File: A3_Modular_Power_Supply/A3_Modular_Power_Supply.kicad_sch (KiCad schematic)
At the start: 73 parts, among them J1 JST-XH, J10 JST-XH, J11 JST-XH, J12 JST-XH, J13 JST-XH, J14 JST-XH, J15 JST-XH, J16 JST-XH, J17 FX30B-3P-7.62DSA, J18 FX30B-3S-7.62DSA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

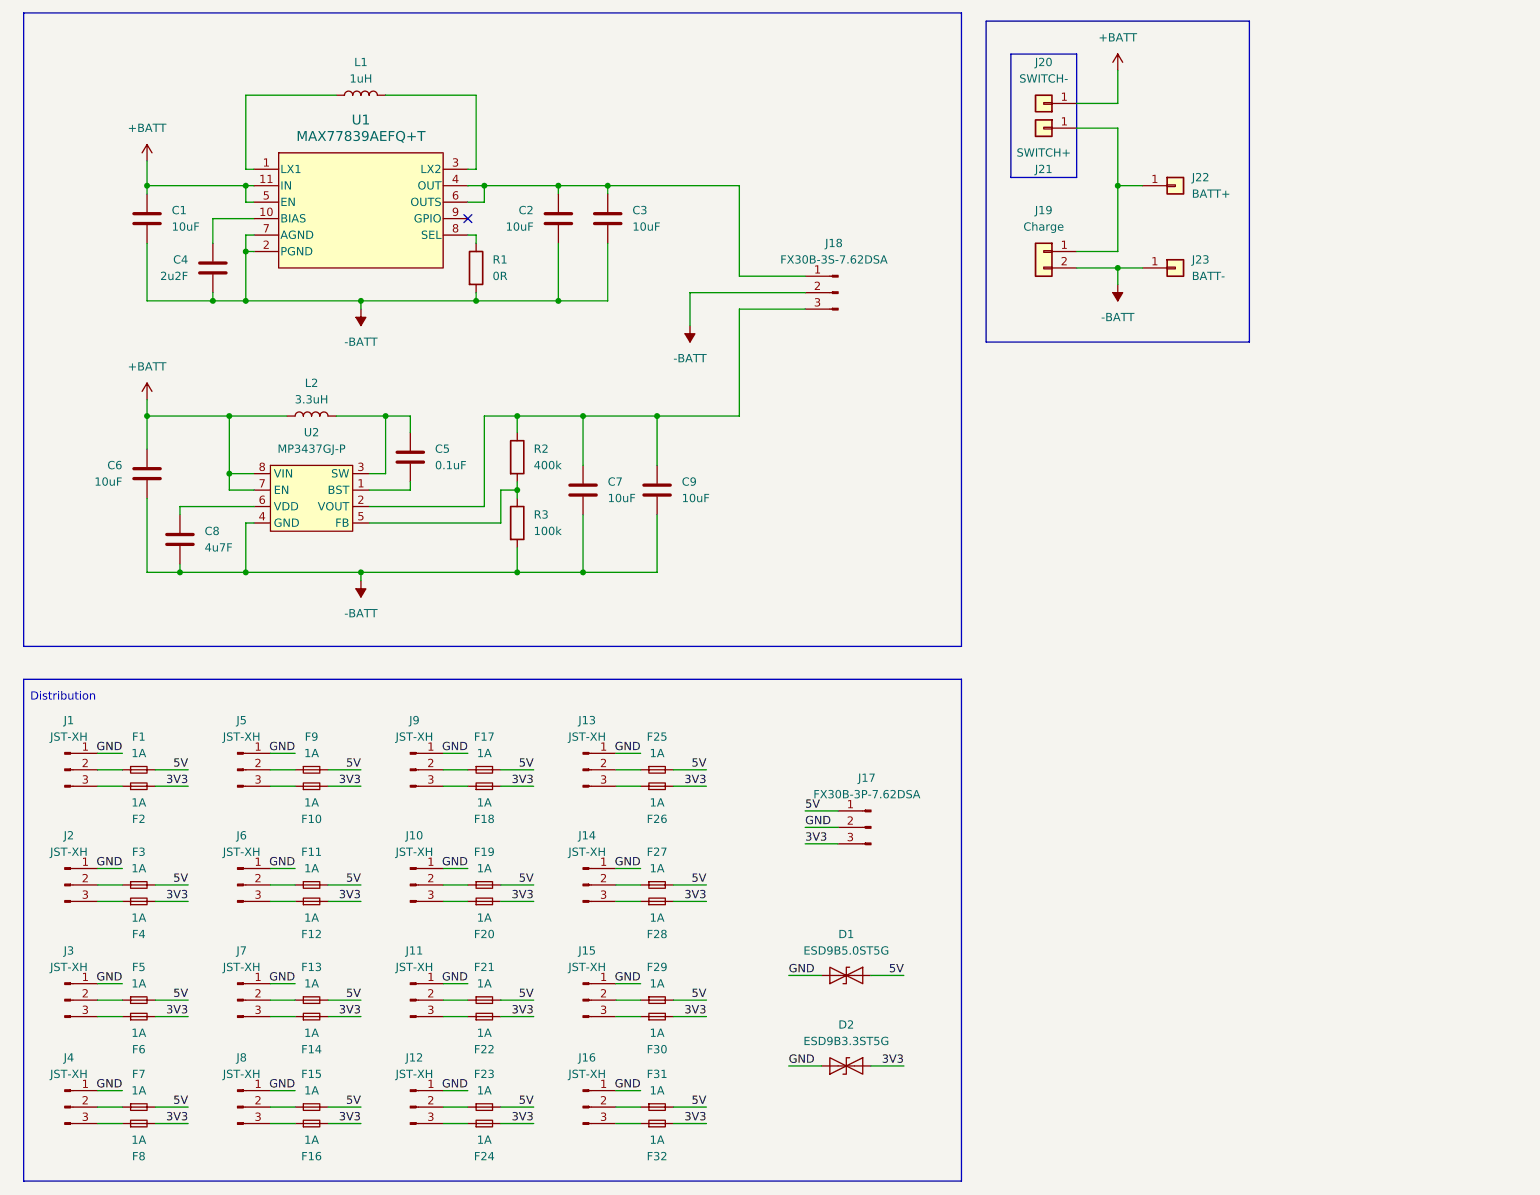
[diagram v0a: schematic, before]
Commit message: Resized board to match flight computer Switched to single PCB
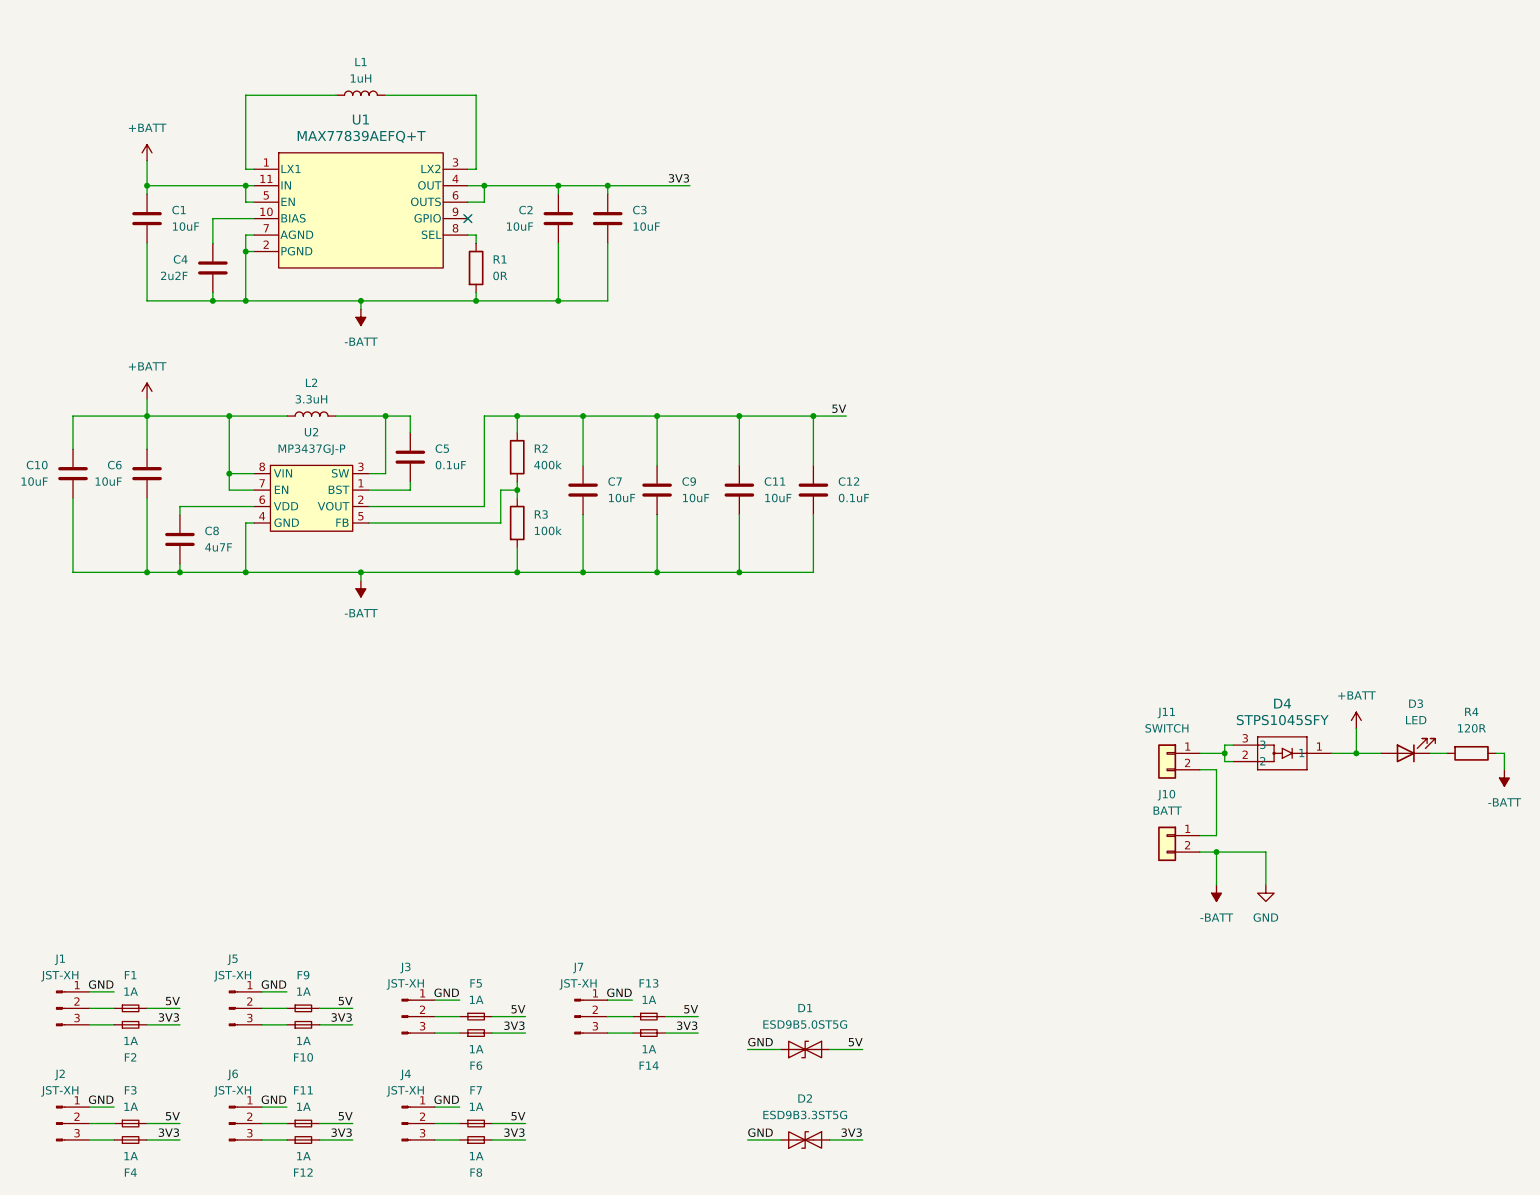
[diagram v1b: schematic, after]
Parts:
- removed F15, F16, F17, F18, F19, F20, F21, F22, F23, F24, F25, F26, F27, F28, F29, F30, F31, F32: 1A, Fuse:Fuse_0603_1608Metric, symbol Device:Fuse_Small
- removed J10, J11, J12, J13, J14, J15, J16, J8, J9: JST-XH, Connector_JST:JST_XH_B3B-XH-A_1x03_P2.50mm_Vertical, symbol Connector:Conn_01x03_Pin
- removed J17: FX30B-3P-7.62DSA, MPS_footprints:FX30B-3x-7.62, symbol Connector:Conn_01x03_Pin
- removed J18: FX30B-3S-7.62DSA, MPS_footprints:FX30B-3x-7.62, symbol Connector:Conn_01x03_Pin
- removed J20: SWITCH-, Connector_Wire:SolderWire-1.5sqmm_1x01_D1.7mm_OD3.9mm, symbol Connector_Generic:Conn_01x01
- removed J21: SWITCH+, Connector_Wire:SolderWire-1.5sqmm_1x01_D1.7mm_OD3.9mm, symbol Connector_Generic:Conn_01x01
- removed J22: BATT+, MPS_footprints:Nickle_Strip, symbol Connector_Generic:Conn_01x01
- removed J23: BATT-, MPS_footprints:Nickle_Strip, symbol Connector_Generic:Conn_01x01
- added C10, C11: 10uF, Capacitor_SMD:C_1206_3216Metric, symbol Device:C
- added C12: 0.1uF, Capacitor_SMD:C_0603_1608Metric, symbol Device:C
- added D3: LED, LED_SMD:LED_0603_1608Metric, symbol Device:LED
- added D4: STPS1045SFY, PSMCTO-277A_STM, symbol MPS_symbols:STPS1045SFY
- added J11: SWITCH, Connector_JST:JST_VH_B2PS-VH_1x02_P3.96mm_Horizontal, symbol Connector_Generic:Conn_01x02
- added R4: 120R, Resistor_SMD:R_0603_1608Metric, symbol Device:R
- J1, J2, J3, J4, J5, J6, J7: footprint Connector_JST:JST_XH_B3B-XH-A_1x03_P2.50mm_Vertical -> Connector_JST:JST_XH_S3B-XH-A_1x03_P2.50mm_Horizontal
- J10: renamed from J19; value Charge -> BATT
- L2: footprint Inductor_SMD:L_Bourns_SRP1245A -> MPS_footprints:L_Wurth_WE-XHMI-6060P
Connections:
- net GND is gone; now on net -BATT: D1.2 (A2), D2.1 (A1), J1.1 (Pin_1), J2.1 (Pin_1), J3.1 (Pin_1), J4.1 (Pin_1), J5.1 (Pin_1), J6.1 (Pin_1), J7.1 (Pin_1)
- net +BATT: now also C10.1, D3.2 (A), D4.1
- net -BATT: now also C10.2, C11.2, C12.2, R4.1
- net 3V3: now also C2.1, C3.1, U1.4 (OUT), U1.6 (OUTS)
- net 5V: now also C7.1, C9.1, R2.1, U2.2 (VOUT), C11.1, C12.1
- net at J10.1 (Pin_1): now also J11.2 (Pin_2)
- new net: D3.1 (K), R4.2
- new net: D4.2, D4.3, J11.1 (Pin_1)
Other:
- note removed: "Distribution"
- moved on the sheet: D1, D2, F1, F10, F11, F12, F13, F14, F2, F3, F4, F5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

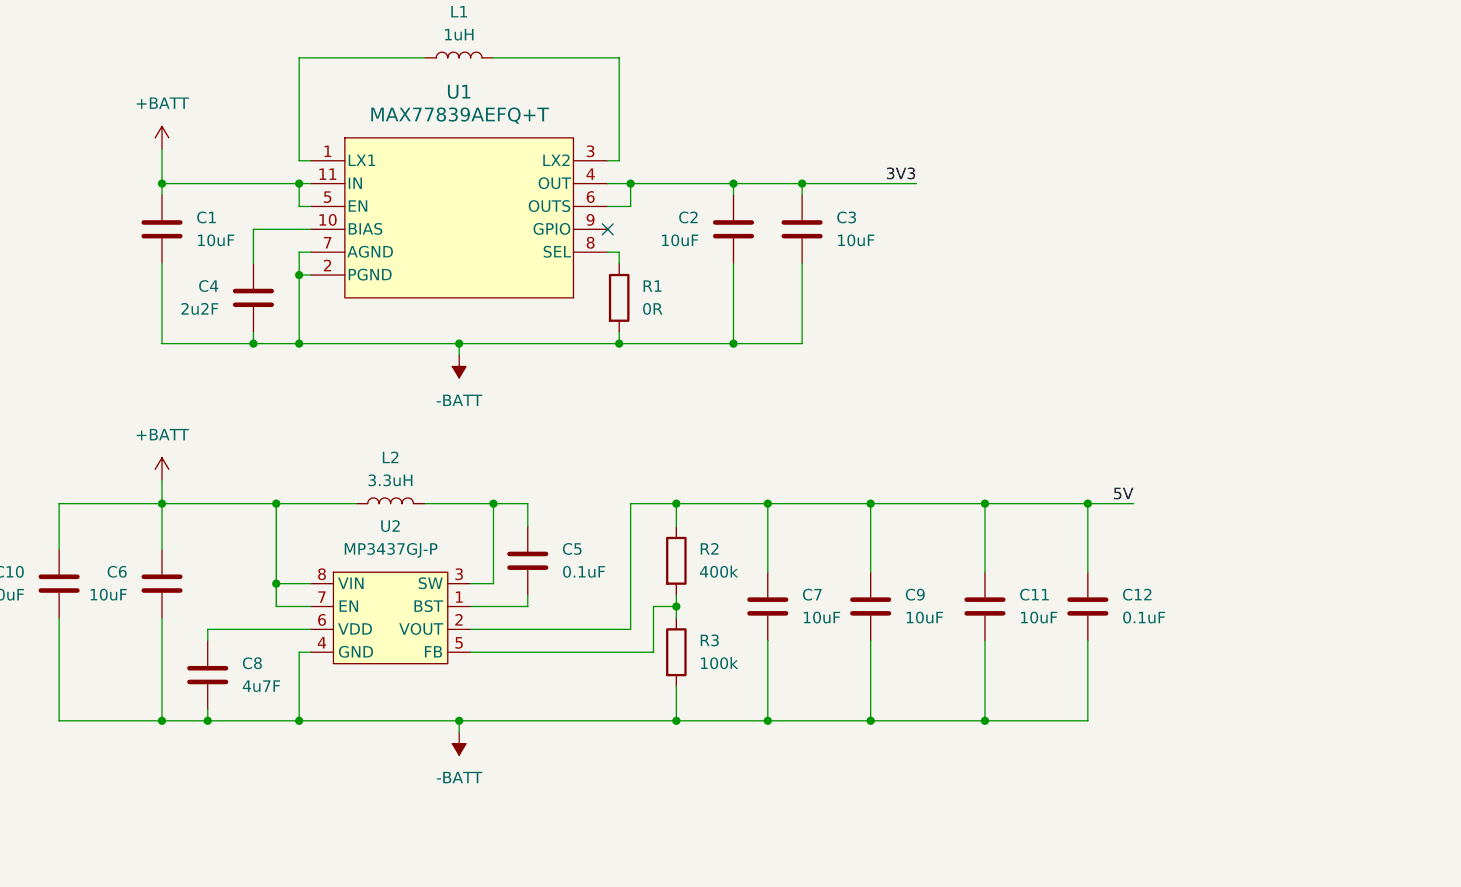
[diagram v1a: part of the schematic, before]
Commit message: Added power indication LEDs
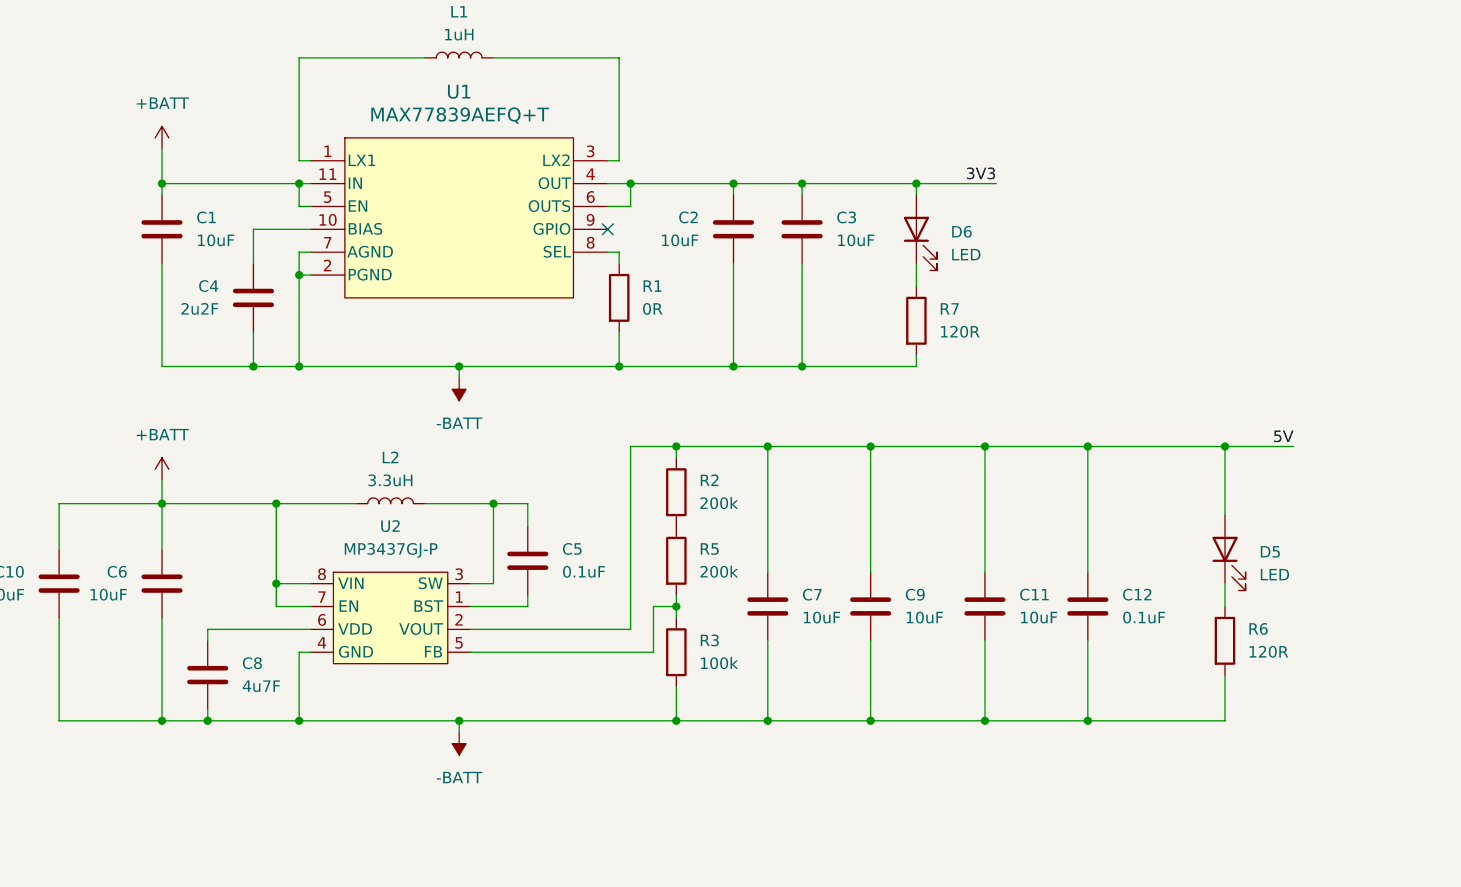
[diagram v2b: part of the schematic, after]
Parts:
- added D5, D6: LED, LED_SMD:LED_0603_1608Metric, symbol Device:LED
- added R5: 200k, Resistor_SMD:R_0603_1608Metric, symbol Device:R
- added R6, R7: 120R, Resistor_SMD:R_0603_1608Metric, symbol Device:R
- R2: value 400k -> 200k
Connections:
- net -BATT: now also R6.2, R7.2
- net 3V3: now also D6.2 (A)
- net 5V: now also D5.2 (A)
- net at R3.1, U2.5 (FB): now also R5.2; no longer R2.2
- new net: D5.1 (K), R6.1
- new net: R2.2, R5.1
- new net: D6.1 (K), R7.1
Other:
- moved on the sheet: R2
